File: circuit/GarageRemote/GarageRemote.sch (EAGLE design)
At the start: 11 parts, among them U1 ESP32-DEVKITC, U2 ILQ30-X001

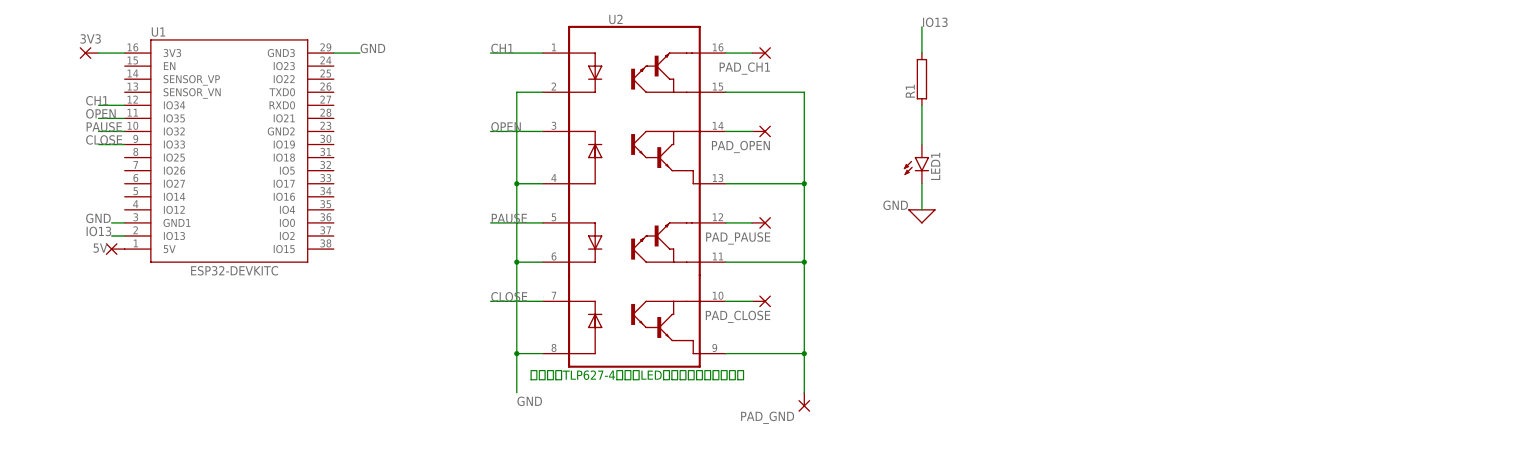
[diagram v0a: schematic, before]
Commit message: Ver1.3に改修しました。
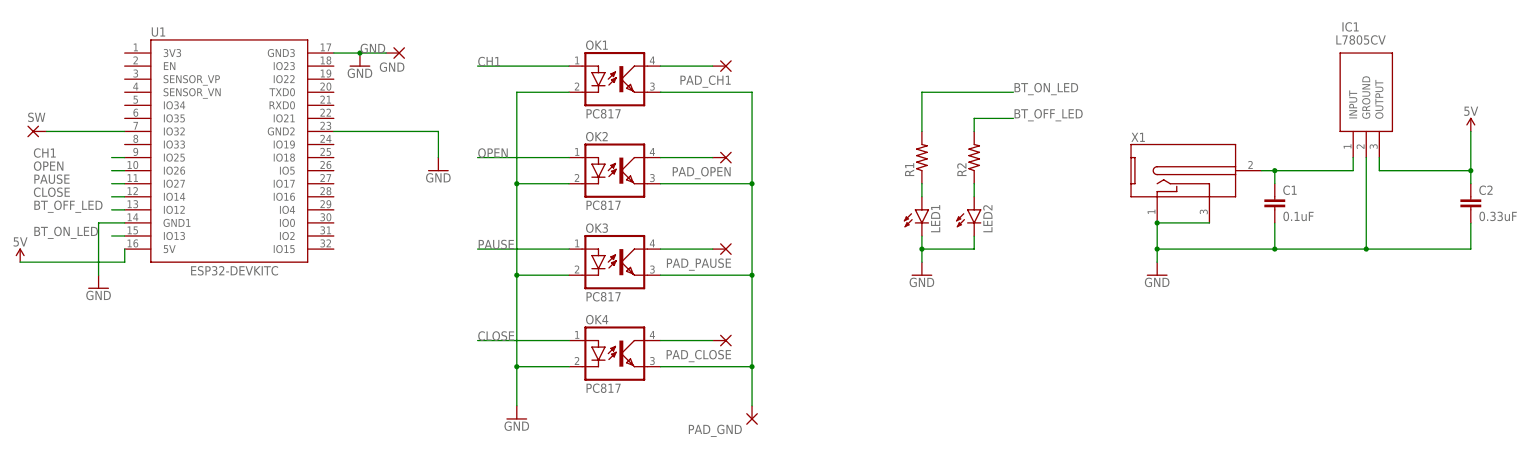
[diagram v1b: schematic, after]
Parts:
- removed 3V3, 5V: (no value), wirepad:2,54/1,0
- removed U2: ILQ30-X001, ILQ30-X001:ILQ30-X001
- added C1: 0.1uF, capacitor-wima:C2.5/2
- added C2: 0.33uF, capacitor-wima:C2.5/2
- added GND, SW: (no value), wirepad:2,54/1,0
- added IC1: L7805CV, L7805CV:L7805CV
- added LED2: (no value), led:LED5MM
- added OK1, OK2, OK3, OK4: PC817, optocoupler:PC817
- added R2: (no value), resistor:R-US_0204/5
- added X1: (no value), power-jack:DC-2.1MM-5MM
- R1: device resistor-power:RCA0001 -> resistor:R-US_0204/5
- U1: device ESP32-DEVKITC:ESP32-DEVKITC -> AE-ESP32-WROOM-32E-MINI:ESP32-DEVKITC
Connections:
- net IO13 renamed BT_ON_LED
- removed net N$9 (its old number): 3V3.P, U1.3V3
- new net 5V: C2.1, IC1.OUTPUT, U1.5V
- new net BT_OFF_LED: R2.2, U1.IO12
- new net N$6: SW.P, U1.IO32
- new net N$7: LED2.A, R2.1
- net CH1: now also OK1.A, U1.IO25; no longer U1.IO34, U2.1
- net CLOSE: now also OK4.A, U1.IO14; no longer U1.IO33, U2.7.
- net GND: now also C1.2, C2.2, GND.P, IC1.GROUND, LED2.C, OK1.C, OK2.C, OK3.C, OK4.C, U1.GND2, X1.1, X1.2; no longer U2.2, U2.4, U2.6., U2.8.
- net N$1: now also OK1.EMIT, OK2.EMIT, OK3.EMIT, OK4.EMIT; no longer U2.11, U2.13, U2.15, U2.9.
- net N$2: now also OK2.COL; no longer U2.14
- net N$3: now also OK1.COL; no longer U2.16
- net N$4: now also OK3.COL; no longer U2.12
- net N$5: now also OK4.COL; no longer U2.10
- net N$8: now also C1.1, IC1.INPUT, X1.3; no longer 5V.P, U1.5V
- net OPEN: now also OK2.A, U1.IO26; no longer U1.IO35, U2.3
- net PAUSE: now also OK3.A, U1.IO27; no longer U1.IO32, U2.5.
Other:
- note removed: "本当は、TLP627-4だからLEDの向きを無視している"
- moved on the sheet: LED1, PAD_CH1, PAD_CLOSE, PAD_GND, PAD_OPEN, PAD_PAUSE
